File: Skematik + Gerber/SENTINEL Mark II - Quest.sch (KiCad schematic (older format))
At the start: 22 parts, among them J10 External, J7 SERVO1, J8 SERVO2, J9 SENSOR, U3 STM32F103CBTx, Y1 8MHz/20pF

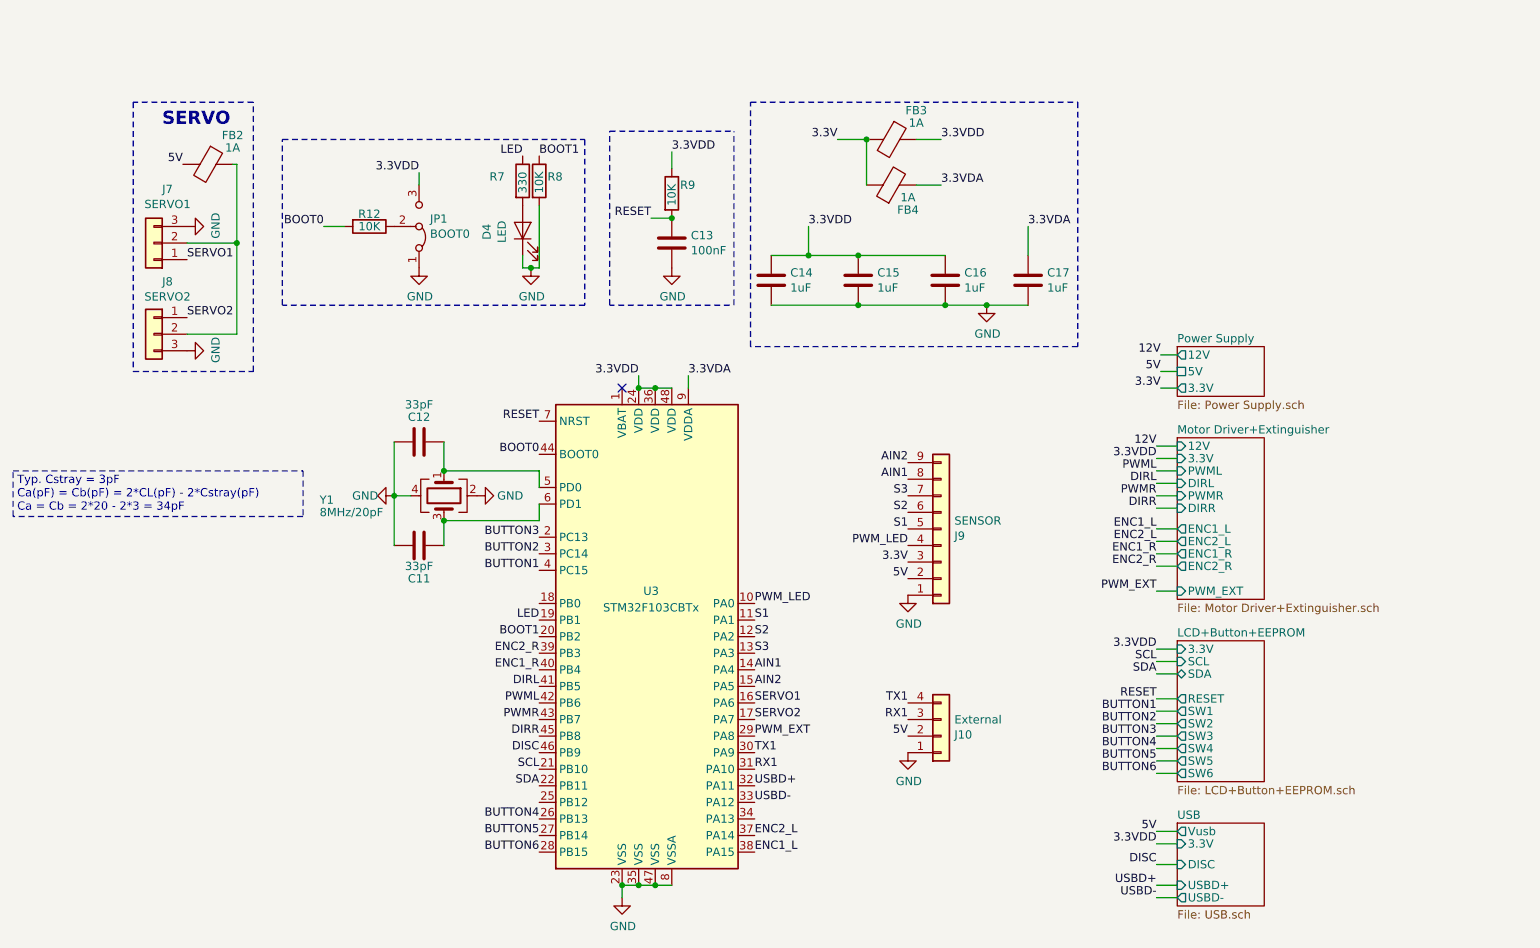
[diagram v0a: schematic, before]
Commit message: sensor Schematic added
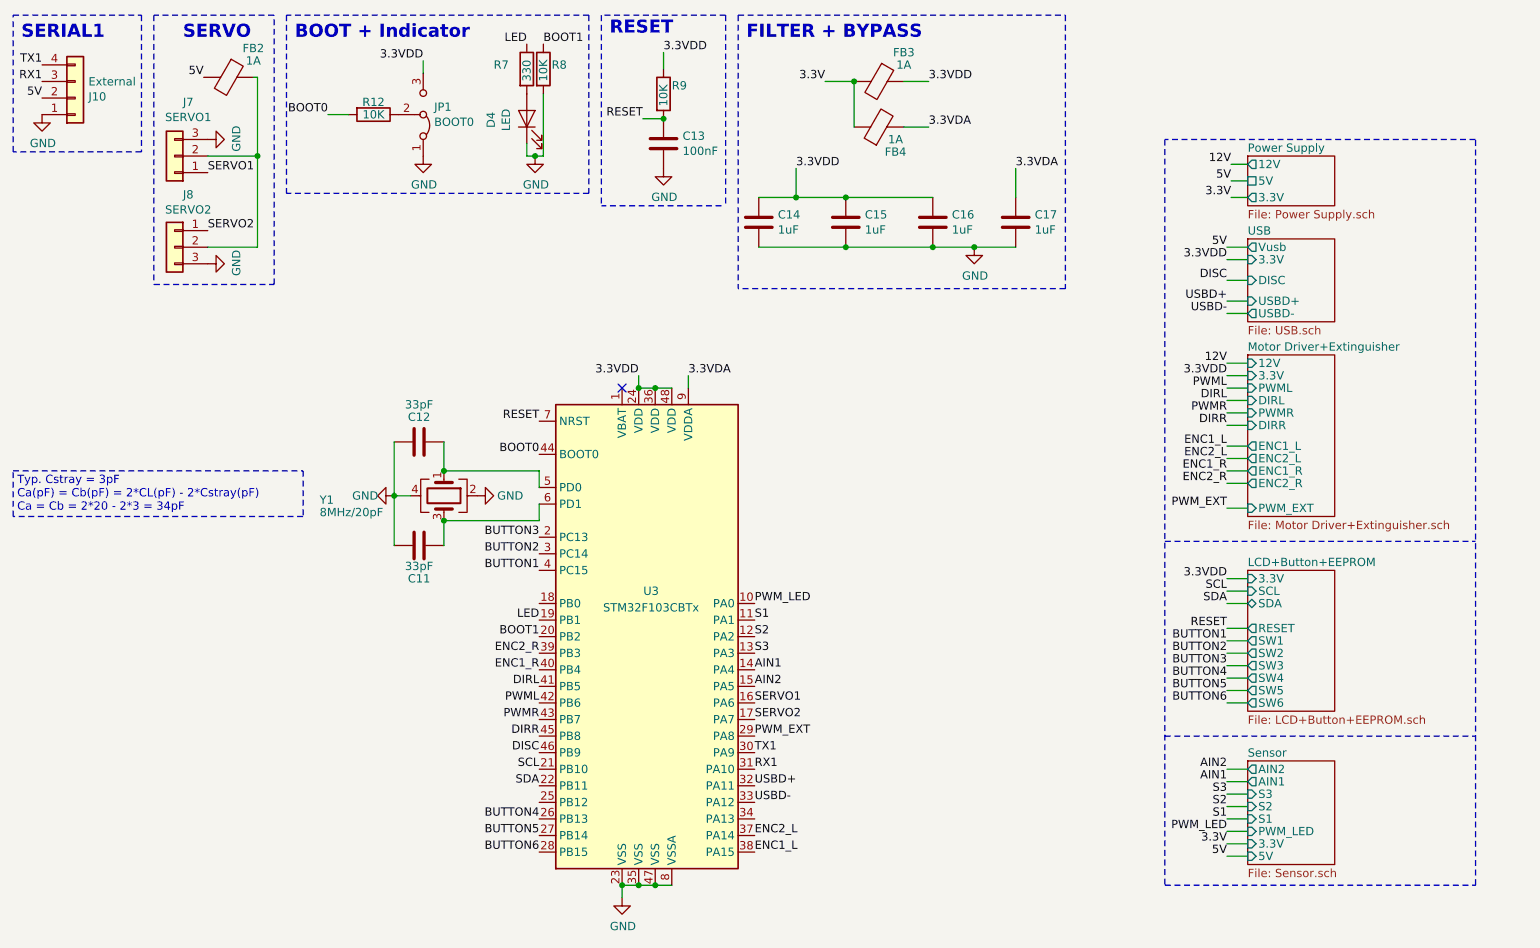
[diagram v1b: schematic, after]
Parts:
- removed J9: SENSOR, Connector_JST:JST_PH_S9B-PH-K_1x09_P2.00mm_Horizontal, symbol Connector_Generic:Conn_01x09
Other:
- note added: "BOOT + Indicator"
- note added: "FILTER + BYPASS"
- note added: "RESET"
- note added: "SERIAL1"
- moved on the sheet: C13, C14, C15, C16, C17, D4, FB2, FB3, FB4, J10, J7, J8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
